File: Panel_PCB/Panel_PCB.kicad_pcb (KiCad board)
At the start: 2 copper layers, 24 parts, among them J1 Screw_Terminal_01x20, J2 Screw_Terminal_01x20, J3 Screw_Terminal_01x20, J4 Screw_Terminal_01x20

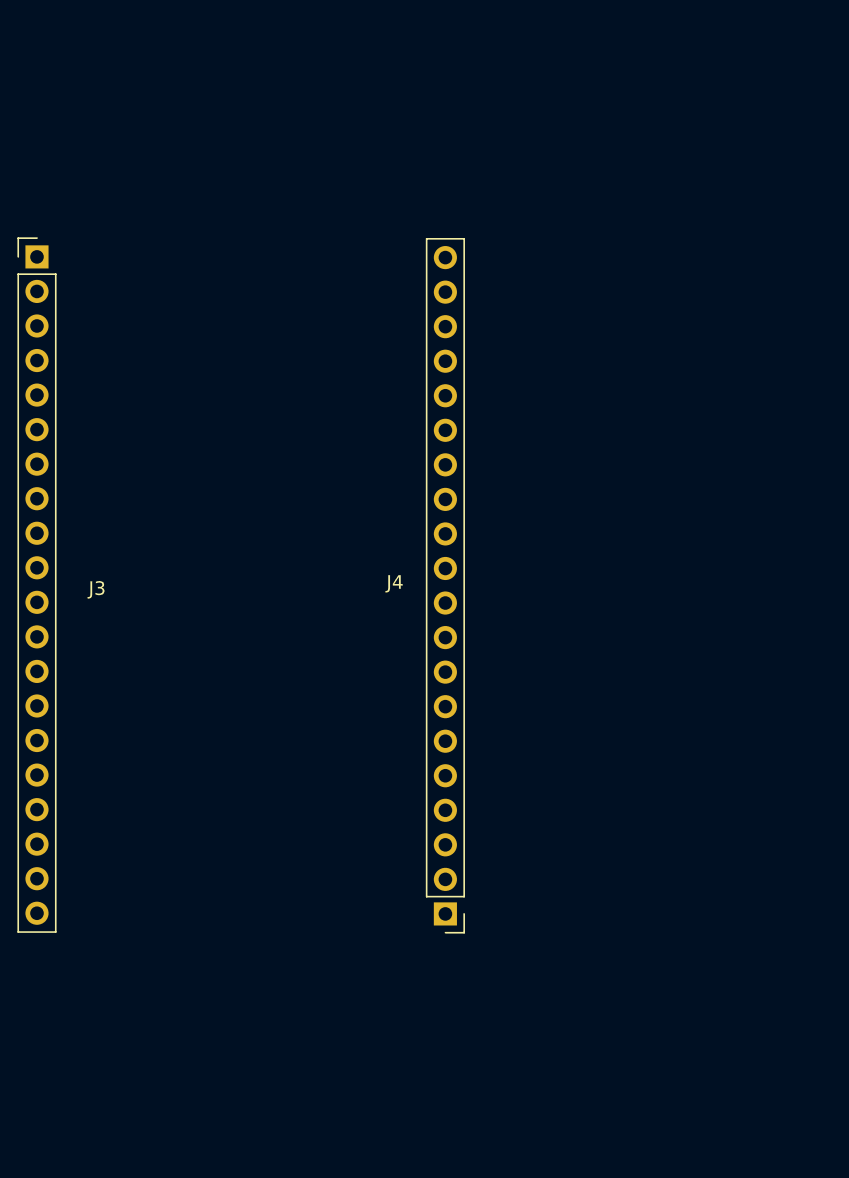
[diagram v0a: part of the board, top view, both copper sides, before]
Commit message: Layout para el esp32 en la placa
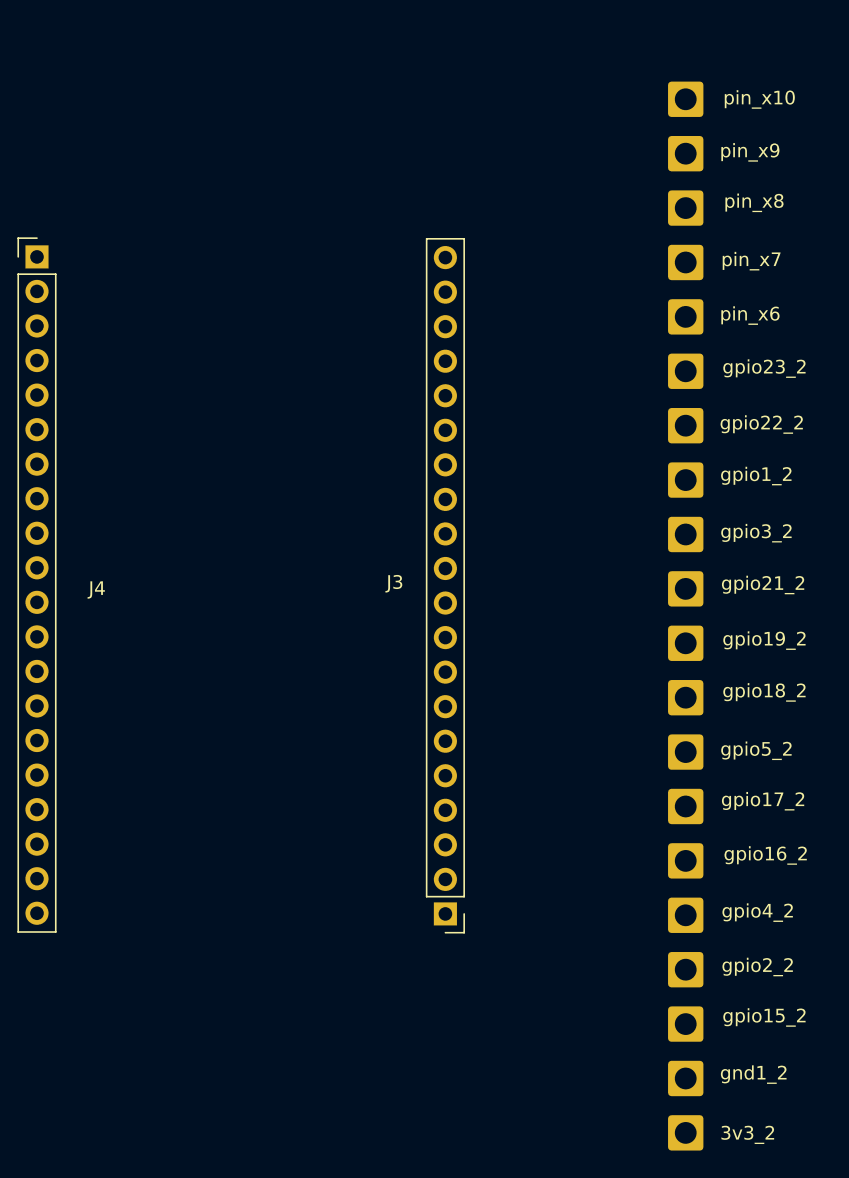
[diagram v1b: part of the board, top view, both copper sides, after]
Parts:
- added 3v3_2: ~, Connector_Wire:SolderWire-0.75sqmm_1x01_D1.25mm_OD2.3mm, F.Cu at (180.7, 193.9)
- added gnd1_2: ~, Connector_Wire:SolderWire-0.75sqmm_1x01_D1.25mm_OD2.3mm, F.Cu at (180.7, 189.9)
- added gpio15_2: ~, Connector_Wire:SolderWire-0.75sqmm_1x01_D1.25mm_OD2.3mm, F.Cu at (180.7, 185.9)
- added gpio16_2: ~, Connector_Wire:SolderWire-0.75sqmm_1x01_D1.25mm_OD2.3mm, F.Cu at (180.7, 173.9)
- added gpio17_2: ~, Connector_Wire:SolderWire-0.75sqmm_1x01_D1.25mm_OD2.3mm, F.Cu at (180.7, 169.9)
- added gpio18_2: ~, Connector_Wire:SolderWire-0.75sqmm_1x01_D1.25mm_OD2.3mm, F.Cu at (180.7, 161.9)
- added gpio19_2: ~, Connector_Wire:SolderWire-0.75sqmm_1x01_D1.25mm_OD2.3mm, F.Cu at (180.7, 157.9)
- added gpio1_2: ~, Connector_Wire:SolderWire-0.75sqmm_1x01_D1.25mm_OD2.3mm, F.Cu at (180.7, 145.9)
- added gpio21_2: ~, Connector_Wire:SolderWire-0.75sqmm_1x01_D1.25mm_OD2.3mm, F.Cu at (180.7, 153.9)
- added gpio22_2: ~, Connector_Wire:SolderWire-0.75sqmm_1x01_D1.25mm_OD2.3mm, F.Cu at (180.7, 141.9)
- added gpio23_2: ~, Connector_Wire:SolderWire-0.75sqmm_1x01_D1.25mm_OD2.3mm, F.Cu at (180.7, 137.9)
- added gpio2_2: ~, Connector_Wire:SolderWire-0.75sqmm_1x01_D1.25mm_OD2.3mm, F.Cu at (180.7, 181.9)
- added gpio3_2: ~, Connector_Wire:SolderWire-0.75sqmm_1x01_D1.25mm_OD2.3mm, F.Cu at (180.7, 149.9)
- added gpio4_2: ~, Connector_Wire:SolderWire-0.75sqmm_1x01_D1.25mm_OD2.3mm, F.Cu at (180.7, 177.9)
- added gpio5_2: ~, Connector_Wire:SolderWire-0.75sqmm_1x01_D1.25mm_OD2.3mm, F.Cu at (180.7, 165.9)
- added pin_x10: ~, Connector_Wire:SolderWire-0.75sqmm_1x01_D1.25mm_OD2.3mm, F.Cu at (180.7, 118.0)
- added pin_x6: ~, Connector_Wire:SolderWire-0.75sqmm_1x01_D1.25mm_OD2.3mm, F.Cu at (180.7, 133.9)
- added pin_x7: ~, Connector_Wire:SolderWire-0.75sqmm_1x01_D1.25mm_OD2.3mm, F.Cu at (180.7, 129.9)
- added pin_x8: ~, Connector_Wire:SolderWire-0.75sqmm_1x01_D1.25mm_OD2.3mm, F.Cu at (180.7, 126.0)
- added pin_x9: ~, Connector_Wire:SolderWire-0.75sqmm_1x01_D1.25mm_OD2.3mm, F.Cu at (180.7, 122.0)
- renumbered J4 to J3, J3 to J4
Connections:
- J3 pad 1: unconnected-(J4-Pin_1-Pad1) (its old number) -> Net-(3v3_2-Pin_1)
- J3 pad 10: unconnected-(J4-Pin_10-Pad10) (its old number) -> Net-(J3-Pin_10)
- J3 pad 11: unconnected-(J4-Pin_11-Pad11) (its old number) -> Net-(J3-Pin_11)
- J3 pad 12: unconnected-(J4-Pin_12-Pad12) (its old number) -> Net-(J3-Pin_12)
- J3 pad 13: unconnected-(J4-Pin_13-Pad13) (its old number) -> Net-(J3-Pin_13)
- J3 pad 14: unconnected-(J4-Pin_14-Pad14) (its old number) -> Net-(J3-Pin_14)
- J3 pad 15: unconnected-(J4-Pin_15-Pad15) (its old number) -> Net-(J3-Pin_15)
- J3 pad 16: unconnected-(J4-Pin_16-Pad16) (its old number) -> Net-(J3-Pin_16)
- J3 pad 17: unconnected-(J4-Pin_17-Pad17) (its old number) -> Net-(J3-Pin_17)
- J3 pad 18: unconnected-(J4-Pin_18-Pad18) (its old number) -> Net-(J3-Pin_18)
- J3 pad 19: unconnected-(J4-Pin_19-Pad19) (its old number) -> Net-(J3-Pin_19)
- J3 pad 2: unconnected-(J4-Pin_2-Pad2) (its old number) -> Net-(J3-Pin_2)
- J3 pad 20: unconnected-(J4-Pin_20-Pad20) (its old number) -> Net-(J3-Pin_20)
- J3 pad 3: unconnected-(J4-Pin_3-Pad3) (its old number) -> Net-(J3-Pin_3)
- J3 pad 4: unconnected-(J4-Pin_4-Pad4) (its old number) -> Net-(J3-Pin_4)
- J3 pad 5: unconnected-(J4-Pin_5-Pad5) (its old number) -> Net-(J3-Pin_5)
- J3 pad 6: unconnected-(J4-Pin_6-Pad6) (its old number) -> Net-(J3-Pin_6)
- J3 pad 7: unconnected-(J4-Pin_7-Pad7) (its old number) -> Net-(J3-Pin_7)
- J3 pad 8: unconnected-(J4-Pin_8-Pad8) (its old number) -> Net-(J3-Pin_8)
- J3 pad 9: unconnected-(J4-Pin_9-Pad9) (its old number) -> Net-(J3-Pin_9)

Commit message: Recursos útiles para el diseño electrónico
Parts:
- added C1: C_US, Capacitor_THT:C_Radial_D18.0mm_H35.5mm_P7.50mm, F.Cu at (3.20, 110.3)
- added D1: D_Bridge_+AA-, Diode_THT:Diode_Bridge_19.0x3.5x10.0mm_P5.0mm, F.Cu at (-52.2, 117.5)
- added D2: D_Zener, Diode_THT:D_A-405_P7.62mm_Horizontal, F.Cu at (69.0, 112.8)
- added K1: SANYOU_SRD_Form_C, Relay_THT:Relay_SPDT_SANYOU_SRD_Series_Form_C, F.Cu at (255.6, 138.7)
- added R1: R_US, Resistor_THT:R_Axial_DIN0617_L17.0mm_D6.0mm_P30.48mm_Horizontal, F.Cu at (-37.9, 94.3)
- added R2: R_US, Resistor_THT:R_Axial_DIN0617_L17.0mm_D6.0mm_P30.48mm_Horizontal, F.Cu at (28.4, 97.0)
- added U1: 4N35, Package_DIP:DIP-6_W7.62mm, F.Cu at (229.6, 46.1)
- added U2: ESP32-WROOM-32, RF_Module:ESP32-WROOM-32, F.Cu at (251.8, -2.36)
- added U3: CH340C, Package_SO:SOIC-16_3.9x9.9mm_P1.27mm, F.Cu at (237.7, 100.4)
- added U4: LM1117T-3.3, Package_TO_SOT_THT:TO-220-3_Horizontal_TabDown, F.Cu at (127.3, 117.2)
- added U6: LM7812_TO220, Package_TO_SOT_THT:TO-220-3_Vertical, F.Cu at (97.2, 106.7)
- moved 3v3_2 174.8 mm to (72.6, 56.6)
- moved J3 174.8 mm to (55.0, 40.5)
- moved J4 174.8 mm to (24.9, -7.80)
- moved gnd1_2 174.8 mm to (72.6, 52.6)
- moved gpio15_2 174.8 mm to (72.6, 48.6)
- moved gpio16_2 174.8 mm to (72.6, 36.6)
- moved gpio17_2 174.8 mm to (72.6, 32.6)
- moved gpio18_2 174.8 mm to (72.6, 24.6)
- moved gpio19_2 174.8 mm to (72.6, 20.6)
- moved gpio1_2 174.8 mm to (72.6, 8.61)
- moved gpio21_2 174.8 mm to (72.6, 16.6)
- moved gpio22_2 174.8 mm to (72.6, 4.61)
- moved gpio23_2 174.8 mm to (72.6, 0.61)
- moved gpio2_2 174.8 mm to (72.6, 44.6)
- moved gpio3_2 174.8 mm to (72.6, 12.6)
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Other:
- board text added: "Bojtronic"
- board text added: "Security Software"

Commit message: Huellas y valores a componentes
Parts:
- added C10: 100 μF, Capacitor_THT:C_Disc_D3.0mm_W1.6mm_P2.50mm, F.Cu at (-102.8, 34.5)
- added C11: 10 μF, Capacitor_THT:C_Disc_D3.0mm_W1.6mm_P2.50mm, F.Cu at (-102.8, 37.6)
- added C12: 0.22 μF, Capacitor_THT:C_Disc_D3.0mm_W1.6mm_P2.50mm, F.Cu at (-102.8, 40.8)
- added C13: 0.1 μF, Capacitor_THT:C_Disc_D3.0mm_W1.6mm_P2.50mm, F.Cu at (-102.8, 43.9)
- added C2: 0.22 μF, Capacitor_THT:C_Disc_D3.0mm_W1.6mm_P2.50mm, F.Cu at (-114.2, 34.5)
- added C3: 0.1 μF, Capacitor_THT:C_Disc_D3.0mm_W1.6mm_P2.50mm, F.Cu at (-114.2, 37.6)
- added C4: 0.22 μF, Capacitor_THT:C_Disc_D3.0mm_W1.6mm_P2.50mm, F.Cu at (-114.2, 40.8)
- added C5: 0.1 μF, Capacitor_THT:C_Disc_D3.0mm_W1.6mm_P2.50mm, F.Cu at (-114.2, 43.9)
- added C6: 0.22 μF, Capacitor_THT:C_Disc_D3.0mm_W1.6mm_P2.50mm, F.Cu at (-108.5, 34.5)
- added C7: 0.1 μF, Capacitor_THT:C_Disc_D3.0mm_W1.6mm_P2.50mm, F.Cu at (-108.5, 37.6)
- added C8: 100 μF, Capacitor_THT:C_Disc_D3.0mm_W1.6mm_P2.50mm, F.Cu at (-108.5, 40.8)
- added C9: 10 μF, Capacitor_THT:C_Disc_D3.0mm_W1.6mm_P2.50mm, F.Cu at (-108.5, 43.9)
- added D3: 1N4001, Diode_THT:D_DO-41_SOD81_P10.16mm_Horizontal, F.Cu at (-90.8, -6.51)
- added D4: 1N4001, Diode_THT:D_DO-41_SOD81_P10.16mm_Horizontal, F.Cu at (-90.8, -2.27)
- added D5: 1N4001, Diode_THT:D_DO-41_SOD81_P10.16mm_Horizontal, F.Cu at (-90.8, 1.99)
- added D6: 1N4001, Diode_THT:D_DO-41_SOD81_P10.16mm_Horizontal, F.Cu at (-90.8, 6.24)
- added D7: 1N4001, Diode_THT:D_DO-41_SOD81_P10.16mm_Horizontal, F.Cu at (-90.8, 10.5)
- added EN1: ~, Connector_Wire:SolderWire-0.75sqmm_1x01_D1.25mm_OD2.3mm, F.Cu at (-113.3, -20.3)
- added F1: Fuse_Small, Fuse:Fuseholder_Cylinder-5x20mm_Schurter_0031_8201_Horizontal_Open, F.Cu at (-113.5, -28.2)
- added F2: Fuse_Small, Fuse:Fuseholder_Cylinder-5x20mm_Schurter_0031_8201_Horizontal_Open, F.Cu at (161.3, 166.9)
- added GND_2: ~, Connector_Wire:SolderWire-0.75sqmm_1x01_D1.25mm_OD2.3mm, F.Cu at (-113.3, -15.6)
- added GPIO12: ~, Connector_Wire:SolderWire-0.75sqmm_1x01_D1.25mm_OD2.3mm, F.Cu at (-113.3, -11.0)
- added GPIO13: ~, Connector_Wire:SolderWire-0.75sqmm_1x01_D1.25mm_OD2.3mm, F.Cu at (-108.5, -20.3)
- added GPIO14: ~, Connector_Wire:SolderWire-0.75sqmm_1x01_D1.25mm_OD2.3mm, F.Cu at (-108.5, -15.6)
- added GPIO25: ~, Connector_Wire:SolderWire-0.75sqmm_1x01_D1.25mm_OD2.3mm, F.Cu at (-108.5, -11.0)
- added GPIO26: ~, Connector_Wire:SolderWire-0.75sqmm_1x01_D1.25mm_OD2.3mm, F.Cu at (-103.6, -20.3)
- added GPIO27: ~, Connector_Wire:SolderWire-0.75sqmm_1x01_D1.25mm_OD2.3mm, F.Cu at (-103.6, -15.6)
- added GPIO32: ~, Connector_Wire:SolderWire-0.75sqmm_1x01_D1.25mm_OD2.3mm, F.Cu at (-103.6, -11.0)
- added GPIO33: ~, Connector_Wire:SolderWire-0.75sqmm_1x01_D1.25mm_OD2.3mm, F.Cu at (-98.8, -20.3)
- added GPIO34: ~, Connector_Wire:SolderWire-0.75sqmm_1x01_D1.25mm_OD2.3mm, F.Cu at (-98.8, -15.6)
- added GPIO35: ~, Connector_Wire:SolderWire-0.75sqmm_1x01_D1.25mm_OD2.3mm, F.Cu at (-98.8, -11.0)
- added GPIO36: ~, Connector_Wire:SolderWire-0.75sqmm_1x01_D1.25mm_OD2.3mm, F.Cu at (-93.9, -20.3)
- added GPIO39: ~, Connector_Wire:SolderWire-0.75sqmm_1x01_D1.25mm_OD2.3mm, F.Cu at (-93.9, -15.6)
- added J16: Boton 2, TerminalBlock_Phoenix:TerminalBlock_Phoenix_MKDS-1,5-2-5.08_1x02_P5.08mm_Horizontal, F.Cu at (19.9, 168.2)
- added J17: Boton 3, TerminalBlock_Phoenix:TerminalBlock_Phoenix_MKDS-1,5-2-5.08_1x02_P5.08mm_Horizontal, F.Cu at (32.1, 144.0)
- added J18: Sensor IN sgn, TerminalBlock_Phoenix:TerminalBlock_Phoenix_MKDS-1,5-2-5.08_1x02_P5.08mm_Horizontal, F.Cu at (32.1, 156.1)
- added J19: Sensor OUT sgn, TerminalBlock_Phoenix:TerminalBlock_Phoenix_MKDS-1,5-2-5.08_1x02_P5.08mm_Horizontal, F.Cu at (32.1, 168.2)
- added J20: Boton 1, TerminalBlock_Phoenix:TerminalBlock_Phoenix_MKDS-1,5-2-5.08_1x02_P5.08mm_Horizontal, F.Cu at (44.3, 144.0)
- added J21: Boton 1 sgn, TerminalBlock_Phoenix:TerminalBlock_Phoenix_MKDS-1,5-2-5.08_1x02_P5.08mm_Horizontal, F.Cu at (44.3, 156.1)
- added J22: Sensor IN, TerminalBlock_Phoenix:TerminalBlock_Phoenix_MKDS-1,5-2-5.08_1x02_P5.08mm_Horizontal, F.Cu at (44.3, 168.2)
- added J23: Sensor OUT, TerminalBlock_Phoenix:TerminalBlock_Phoenix_MKDS-1,5-2-5.08_1x02_P5.08mm_Horizontal, F.Cu at (56.5, 144.0)
- added J24: Boton 2 sgn, TerminalBlock_Phoenix:TerminalBlock_Phoenix_MKDS-1,5-2-5.08_1x02_P5.08mm_Horizontal, F.Cu at (56.5, 156.1)
- added J25: Boton 3 sgn, TerminalBlock_Phoenix:TerminalBlock_Phoenix_MKDS-1,5-2-5.08_1x02_P5.08mm_Horizontal, F.Cu at (56.5, 168.2)
- added J5: AC, TerminalBlock_Phoenix:TerminalBlock_Phoenix_MKDS-1,5-2-5.08_1x02_P5.08mm_Horizontal, F.Cu at (19.9, 144.0)
- added J6: Bateria, TerminalBlock_Phoenix:TerminalBlock_Phoenix_MKDS-1,5-2-5.08_1x02_P5.08mm_Horizontal, F.Cu at (19.9, 156.1)
- added K1: SANYOU_SRD_Form_C, Relay_THT:Relay_SPDT_SANYOU_SRD_Series_Form_C, F.Cu at (-134.8, -25.3)
- added K14: SANYOU_SRD_Form_C, Relay_THT:Relay_SPDT_SANYOU_SRD_Series_Form_C, F.Cu at (-134.8, 42.5)
- added K2: SANYOU_SRD_Form_C, Relay_THT:Relay_SPDT_SANYOU_SRD_Series_Form_C, F.Cu at (-134.8, -8.31)
- added K4: EC2-4.5SNU, Relay_THT:Relay_DPDT_Kemet_EC2_NU, F.Cu at (-96.6, 35.0)
- added K8: SANYOU_SRD_Form_C, Relay_THT:Relay_SPDT_SANYOU_SRD_Series_Form_C, F.Cu at (-134.8, 8.63)
- added K9: SANYOU_SRD_Form_C, Relay_THT:Relay_SPDT_SANYOU_SRD_Series_Form_C, F.Cu at (-134.8, 25.6)
- added Q1: Q_NPN, Package_TO_SOT_THT:TO-92, F.Cu at (31.6, 177.4)
- added Q2: Q_NPN, Package_TO_SOT_THT:TO-92, F.Cu at (31.6, 183.2)
- added Q3: Q_NPN, Package_TO_SOT_THT:TO-92, F.Cu at (31.6, 189.0)
- added Q4: Q_NPN, Package_TO_SOT_THT:TO-92, F.Cu at (31.6, 194.8)
- added R10: 450, Resistor_THT:R_Axial_DIN0207_L6.3mm_D2.5mm_P10.16mm_Horizontal, F.Cu at (17.9, 196.4)
- added R3: 450, Resistor_THT:R_Axial_DIN0207_L6.3mm_D2.5mm_P10.16mm_Horizontal, F.Cu at (160.6, 174.5)
- added R4: R_US, Resistor_THT:R_Axial_DIN0207_L6.3mm_D2.5mm_P10.16mm_Horizontal, F.Cu at (160.6, 178.6)
- added R5: 150, Resistor_THT:R_Axial_DIN0207_L6.3mm_D2.5mm_P10.16mm_Horizontal, F.Cu at (17.9, 176.2)
- added R6: 450, Resistor_THT:R_Axial_DIN0207_L6.3mm_D2.5mm_P10.16mm_Horizontal, F.Cu at (17.9, 180.2)
- added R7: 150, Resistor_THT:R_Axial_DIN0207_L6.3mm_D2.5mm_P10.16mm_Horizontal, F.Cu at (17.9, 184.3)
- added R8: 450, Resistor_THT:R_Axial_DIN0207_L6.3mm_D2.5mm_P10.16mm_Horizontal, F.Cu at (17.9, 188.3)
- added R9: 150, Resistor_THT:R_Axial_DIN0207_L6.3mm_D2.5mm_P10.16mm_Horizontal, F.Cu at (17.9, 192.4)
- added T1: Transformer_1P_1S, Transformer_THT:Transformer_NF_ETAL_1-1_P1200, F.Cu at (-99.6, 19.3)
- added U1: TLP291, Package_SO:SOIC-4_4.55x2.6mm_P1.27mm, F.Cu at (-84.8, 35.0)
- added U15: LM7805_TO220, Package_TO_SOT_THT:TO-220-3_Vertical, F.Cu at (-92.9, 23.2)
- added U16: LM1117T-3.3, Package_TO_SOT_THT:TO-220-3_Horizontal_TabDown, F.Cu at (-112.5, 11.6)
- added U2: TLP291, Package_SO:SOIC-4_4.55x2.6mm_P1.27mm, F.Cu at (-84.8, 39.1)
- added U20: LM1117T-3.3, Package_TO_SOT_THT:TO-220-3_Horizontal_TabDown, F.Cu at (-100.9, 11.6)
- added U21: LM7812_TO220, Package_TO_SOT_THT:TO-220-3_Vertical, F.Cu at (-92.9, 29.2)
- added U3: TLP291, Package_SO:SOIC-4_4.55x2.6mm_P1.27mm, F.Cu at (-84.8, 43.3)
- added U4: LM7805_TO220, Package_TO_SOT_THT:TO-220-3_Vertical, F.Cu at (-92.9, 17.3)
- added U5: TLP291, Package_SO:SOIC-4_4.55x2.6mm_P1.27mm, F.Cu at (-84.8, 47.4)
- added VIN1: ~, Connector_Wire:SolderWire-0.75sqmm_1x01_D1.25mm_OD2.3mm, F.Cu at (-93.9, -11.0)
- C1: value C_US -> 35V 4700μF
- D1: value D_Bridge_+AA- -> KBP204G; footprint Diode_THT:Diode_Bridge_19.0x3.5x10.0mm_P5.0mm -> Diode_THT:Diode_Bridge_Vishay_KBPM
- D2: value D_Zener -> 12 V; footprint Diode_THT:D_A-405_P7.62mm_Horizontal -> Diode_THT:D_DO-41_SOD81_P10.16mm_Horizontal
- R1, R2: value R_US -> 100 Ω 2W; footprint Resistor_THT:R_Axial_DIN0617_L17.0mm_D6.0mm_P30.48mm_Horizontal -> Resistor_THT:R_Axial_DIN0617_L17.0mm_D6.0mm_P25.40mm_Horizontal
- renumbered 3v3_1 to 3V3, gnd1_1 to GND_1, gpio1_1 to GPIO1, gpio15_1 to GPIO15, gpio16_1 to GPIO16, gpio17_1 to GPIO17, gpio18_1 to GPIO18, gpio19_1 to GPIO19, gpio2_1 to GPIO2, gpio21_1 to GPIO21, gpio22_1 to GPIO22, gpio23_1 to GPIO23, gpio3_1 to GPIO3, gpio4_1 to GPIO4, gpio5_1 to GPIO5
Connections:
- 3V3 pad 1: Net-(3v3_1-Pin_1) -> unconnected-(3V3-Pin_1-Pad1)
- C1 pad 1: unconnected-(C1-Pad1) -> Net-(C1-Pad1)
- C1 pad 2: unconnected-(C1-Pad2) -> Net-(D1--)
- D1 pad 1: unconnected-(D1-+-Pad1) -> Net-(D1-+)
- D1 pad 2: unconnected-(D1-Pad2) -> Net-(D1-Pad2)
- D1 pad 3: unconnected-(D1-Pad3) -> Net-(T1-SA)
- D1 pad 4: unconnected-(D1---Pad4) -> Net-(D1--)
- D2 pad 1: unconnected-(D2-K-Pad1) -> Net-(D2-K)
- D2 pad 2: unconnected-(D2-A-Pad2) -> Net-(D1--)
- GND_1 pad 1: Net-(J1-Pin_2) -> Net-(D1--)
- GPIO1 pad 1: Net-(J1-Pin_13) -> unconnected-(GPIO1-Pin_1-Pad1)
- GPIO15 pad 1: Net-(J1-Pin_3) -> unconnected-(GPIO15-Pin_1-Pad1)
- GPIO16 pad 1: Net-(J1-Pin_6) -> unconnected-(GPIO16-Pin_1-Pad1)
- GPIO17 pad 1: Net-(J1-Pin_7) -> unconnected-(GPIO17-Pin_1-Pad1)
- GPIO18 pad 1: Net-(J1-Pin_9) -> unconnected-(GPIO18-Pin_1-Pad1)
- GPIO19 pad 1: Net-(J1-Pin_10) -> unconnected-(GPIO19-Pin_1-Pad1)
- GPIO2 pad 1: Net-(J1-Pin_4) -> unconnected-(GPIO2-Pin_1-Pad1)
- GPIO21 pad 1: Net-(J1-Pin_11) -> unconnected-(GPIO21-Pin_1-Pad1)
- GPIO22 pad 1: Net-(J1-Pin_14) -> unconnected-(GPIO22-Pin_1-Pad1)
- GPIO23 pad 1: Net-(J1-Pin_15) -> unconnected-(GPIO23-Pin_1-Pad1)
- GPIO3 pad 1: Net-(J1-Pin_12) -> unconnected-(GPIO3-Pin_1-Pad1)
- GPIO4 pad 1: Net-(J1-Pin_5) -> unconnected-(GPIO4-Pin_1-Pad1)
- GPIO5 pad 1: Net-(J1-Pin_8) -> unconnected-(GPIO5-Pin_1-Pad1)
- R1 pad 1: unconnected-(R1-Pad1) -> Net-(D1-+)
- R1 pad 2: unconnected-(R1-Pad2) -> Net-(K4-Pad4)
- R2 pad 1: unconnected-(R2-Pad1) -> Net-(C1-Pad1)
- R2 pad 2: unconnected-(R2-Pad2) -> Net-(D2-K)
- U6 pad 1: unconnected-(U6-VI-Pad1) -> Net-(D2-K)
- U6 pad 2: unconnected-(U6-GND-Pad2) -> Net-(D1--)
- U6 pad 3: unconnected-(U6-VO-Pad3) -> Net-(U15-VI)

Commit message: Corrección de errores
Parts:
- added C14: 35V 4700μF, Capacitor_THT:C_Radial_D18.0mm_H35.5mm_P7.50mm, F.Cu at (173.3, 88.4)
- added J1: Relay 1, TerminalBlock_Phoenix:TerminalBlock_Phoenix_MKDS-1,5-2-5.08_1x02_P5.08mm_Horizontal, F.Cu at (1.62, 32.0)
- added J2: Relay 2, TerminalBlock_Phoenix:TerminalBlock_Phoenix_MKDS-1,5-2-5.08_1x02_P5.08mm_Horizontal, F.Cu at (1.62, 44.1)
- added J3: Relay 3, TerminalBlock_Phoenix:TerminalBlock_Phoenix_MKDS-1,5-2-5.08_1x02_P5.08mm_Horizontal, F.Cu at (1.62, 56.3)
- added J4: Relay 4, TerminalBlock_Phoenix:TerminalBlock_Phoenix_MKDS-1,5-2-5.08_1x02_P5.08mm_Horizontal, F.Cu at (1.62, 68.4)
- added J7: AC, TerminalBlock_Phoenix:TerminalBlock_Phoenix_MKDS-1,5-2-5.08_1x02_P5.08mm_Horizontal, F.Cu at (40.9, 47.3)
- added J8: AC, TerminalBlock_Phoenix:TerminalBlock_Phoenix_MKDS-1,5-2-5.08_1x02_P5.08mm_Horizontal, F.Cu at (40.9, 59.4)
- added Q1: 2N2222A, Package_TO_SOT_THT:TO-92, F.Cu at (204.2, 44.4)
- added Q2: 2N2222A, Package_TO_SOT_THT:TO-92, F.Cu at (204.2, 50.1)
- added Q3: 2N2222A, Package_TO_SOT_THT:TO-92, F.Cu at (204.2, 55.9)
- added Q5: 2N2222A, Package_TO_SOT_THT:TO-92, F.Cu at (204.2, 61.7)
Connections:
- C1 pad 1: Net-(C1-Pad1) -> Net-(D2-K)
- D1 pad 3: Net-(T1-SA) -> Net-(J7-Pin_1)
- F1 pad 1: Net-(T1-SB) -> Net-(J7-Pin_2)
- F2 pad 2: Net-(T1-AA) -> Net-(J8-Pin_1)
- K1 pad 1: unconnected-(K1-Pad1) -> Net-(J2-Pin_2)
- K1 pad 3: unconnected-(K1-Pad3) -> Net-(J2-Pin_1)
- K14 pad 2: Net-(T1-AA) -> Net-(J8-Pin_1)
- K2 pad 1: unconnected-(K2-Pad1) -> Net-(J3-Pin_2)
- K2 pad 3: unconnected-(K2-Pad3) -> Net-(J3-Pin_1)
- K4 pad 1: Net-(T1-AA) -> Net-(J8-Pin_1)
- K4 pad 5: Net-(C1-Pad1) -> Net-(K4-Pad5)
- K8 pad 1: unconnected-(K8-Pad1) -> Net-(J1-Pin_2)
- K8 pad 3: unconnected-(K8-Pad3) -> Net-(J1-Pin_1)
- K9 pad 1: unconnected-(K9-Pad1) -> Net-(J4-Pin_2)
- K9 pad 3: unconnected-(K9-Pad3) -> Net-(J4-Pin_1)
- R2 pad 1: Net-(C1-Pad1) -> Net-(K4-Pad5)
- U1 pad 2: unconnected-(U1-Pad2) -> Net-(D1--)
- U2 pad 2: unconnected-(U2-Pad2) -> Net-(D1--)
- U3 pad 2: unconnected-(U3-Pad2) -> Net-(D1--)
- U5 pad 2: unconnected-(U5-Pad2) -> Net-(D1--)
